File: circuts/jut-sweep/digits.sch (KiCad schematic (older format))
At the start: 181 parts, among them Q1 MOSFET_N, Q10 MOSFET_N, Q11 MOSFET_N, Q12 MOSFET_N, Q13 MOSFET_N, Q2 MOSFET_N, Q3 MOSFET_N, Q4 MOSFET_N, Q5 MOSFET_N, Q6 MOSFET_N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

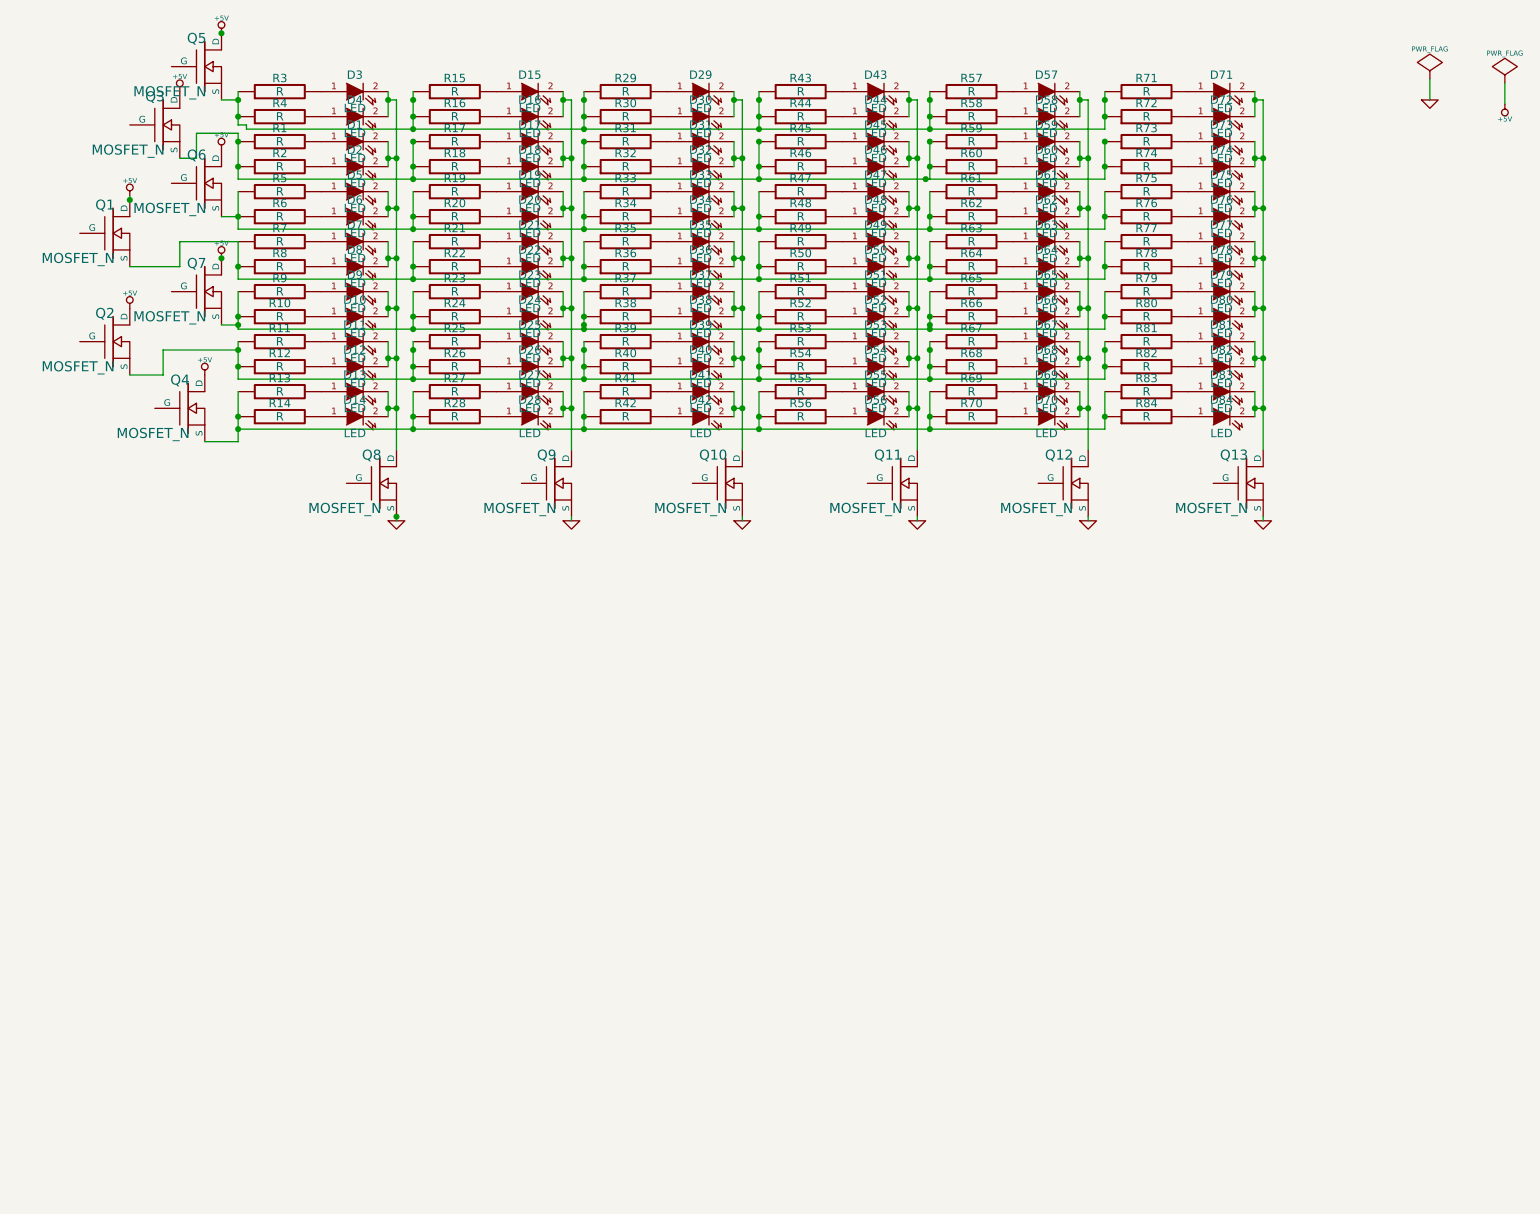
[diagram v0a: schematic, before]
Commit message: Added ATMEGA microcotroller and other (connects and etc..) by masa
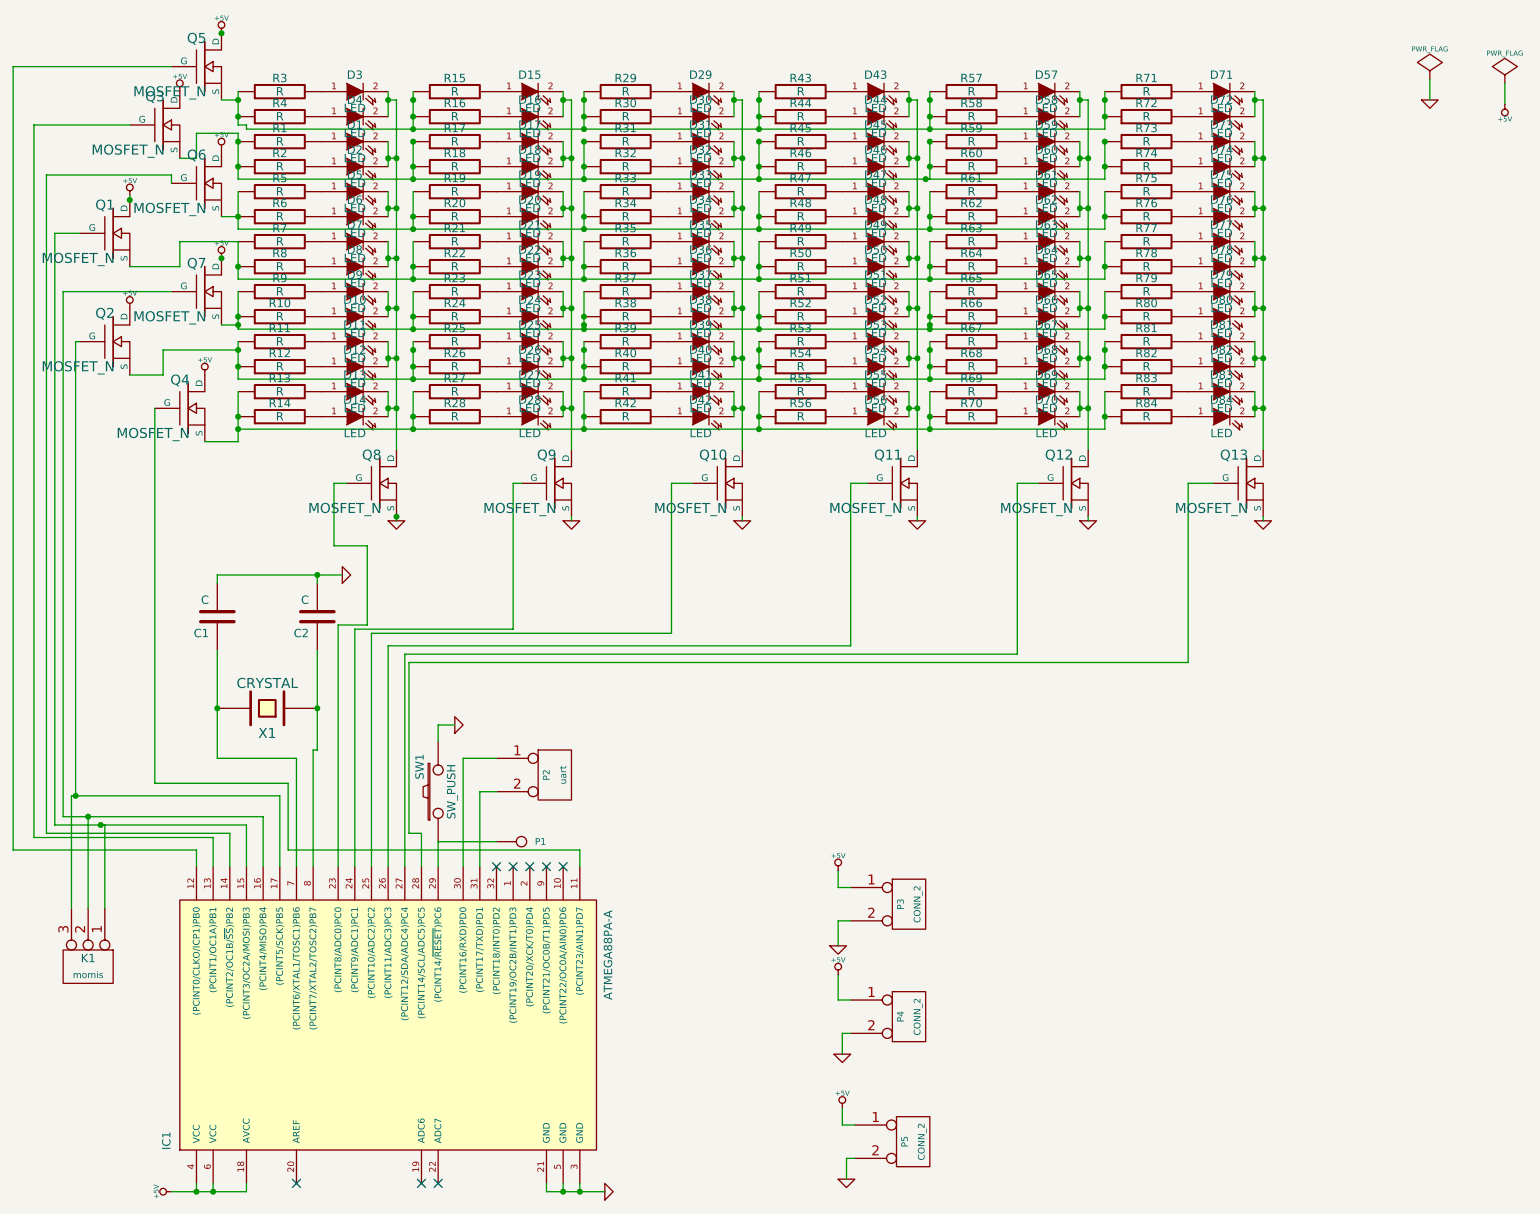
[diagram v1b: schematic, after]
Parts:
- added C1, C2: C, symbol C
- added IC1: ATMEGA88PA-A, TQFP32, symbol ATMEGA88PA-A
- added K1: momis, symbol CONN_3
- added P1: CONN_1, symbol CONN_1
- added P2: uart, symbol CONN_2
- added P3, P4, P5: CONN_2, symbol CONN_2
- added SW1: SW_PUSH, symbol SW_PUSH
- added X1: CRYSTAL, symbol CRYSTAL
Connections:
- net +5V: now also IC1.18 (AVCC), IC1.4 (VCC), IC1.6 (VCC), P3.1 (P1), P4.1 (P1), P5.1 (P1)
- net GND: now also C1.2, C2.2, IC1.21 (GND), IC1.3 (GND), IC1.5 (GND), P3.2 (PM), P4.2 (PM), P5.2 (PM), SW1.2
- net at Q3.G: now also IC1.13 ((PCINT1/OC1A)PB1)
- net at Q6.G: now also IC1.14 ((PCINT2/OC1B/~SS~)PB2)
- net at Q1.G: now also IC1.15 ((PCINT3/OC2A/MOSI)PB3), K1.1 (P1)
- net at Q7.G: now also IC1.16 ((PCINT4/MISO)PB4), K1.2 (PM)
- net at Q2.G: now also IC1.17 ((PCINT5/SCK)PB5), K1.3 (P3)
- net at Q4.G: now also IC1.11 ((PCINT23/AIN1)PD7)
- net at Q9.G: now also IC1.24 ((PCINT9/ADC1)PC1)
- net at Q11.G: now also IC1.26 ((PCINT11/ADC3)PC3)
- net at Q10.G: now also IC1.25 ((PCINT10/ADC2)PC2)
- net at Q12.G: now also IC1.27 ((PCINT12/SDA/ADC4)PC4)
- net at Q13.G: now also IC1.28 ((PCINT14/SCL/ADC5)PC5)
- net at Q8.G: now also IC1.23 ((PCINT8/ADC0)PC0)
- net at Q5.G: now also IC1.12 ((PCINT0/CLKO/ICP1)PB0)
- new net: C2.1, IC1.8 ((PCINT7/XTAL2/TOSC2)PB7), X1.1
- new net: IC1.29 ((PCINT14/~RESET~)PC6), P1.1, SW1.1
- new net: IC1.30 ((PCINT16/RXD)PD0), P2.1 (P1)
- new net: IC1.31 ((PCINT17/TXD)PD1), P2.2 (PM)
- new net: C1.1, IC1.7 ((PCINT6/XTAL1/TOSC1)PB6), X1.2
- no-connect marks 0 -> 8
